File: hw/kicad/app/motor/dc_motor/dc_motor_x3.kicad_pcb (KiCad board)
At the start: 2 copper layers, 45 x 45 mm, 23 parts, among them J1 TOP, J3 Motor 2, J4 Motor 3, J6 BOTTUM, U1 DRV8870DDA, U2 DRV8870DDA, U3 DRV8870DDA

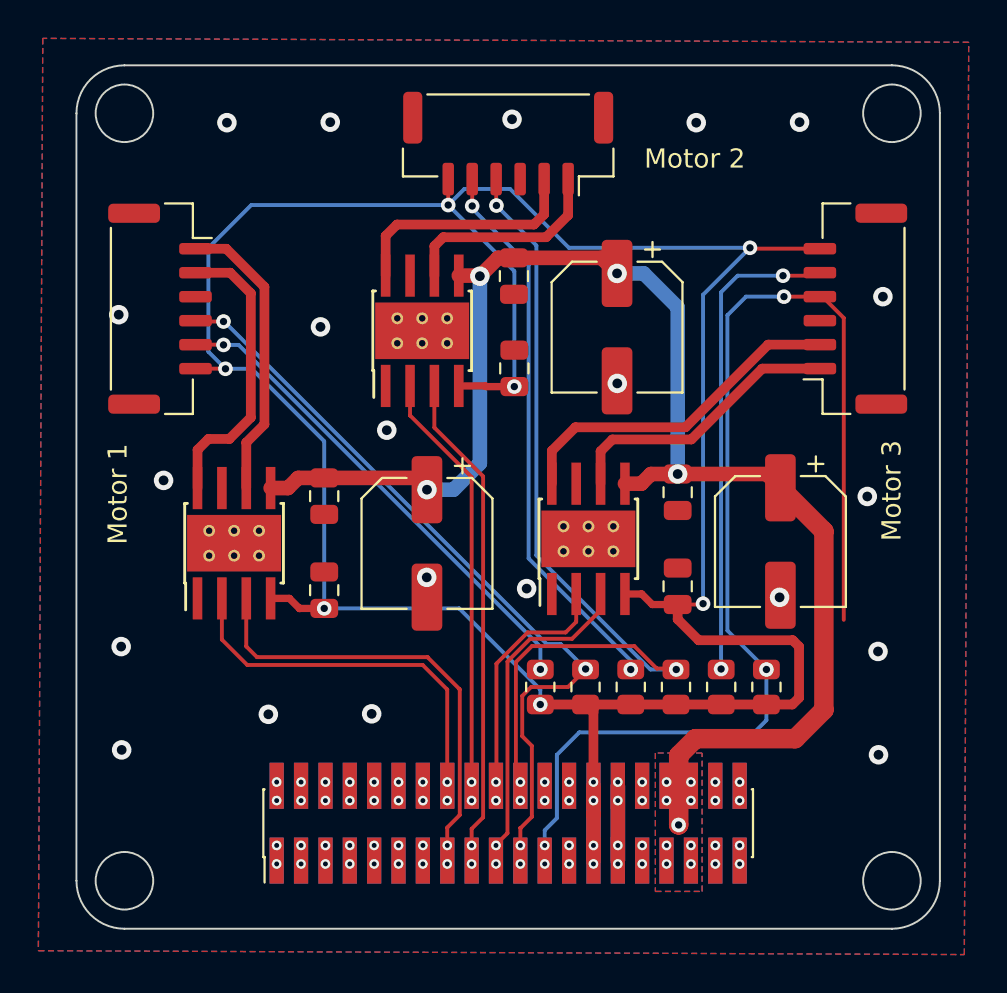
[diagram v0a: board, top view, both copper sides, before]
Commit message: 更换接口线序
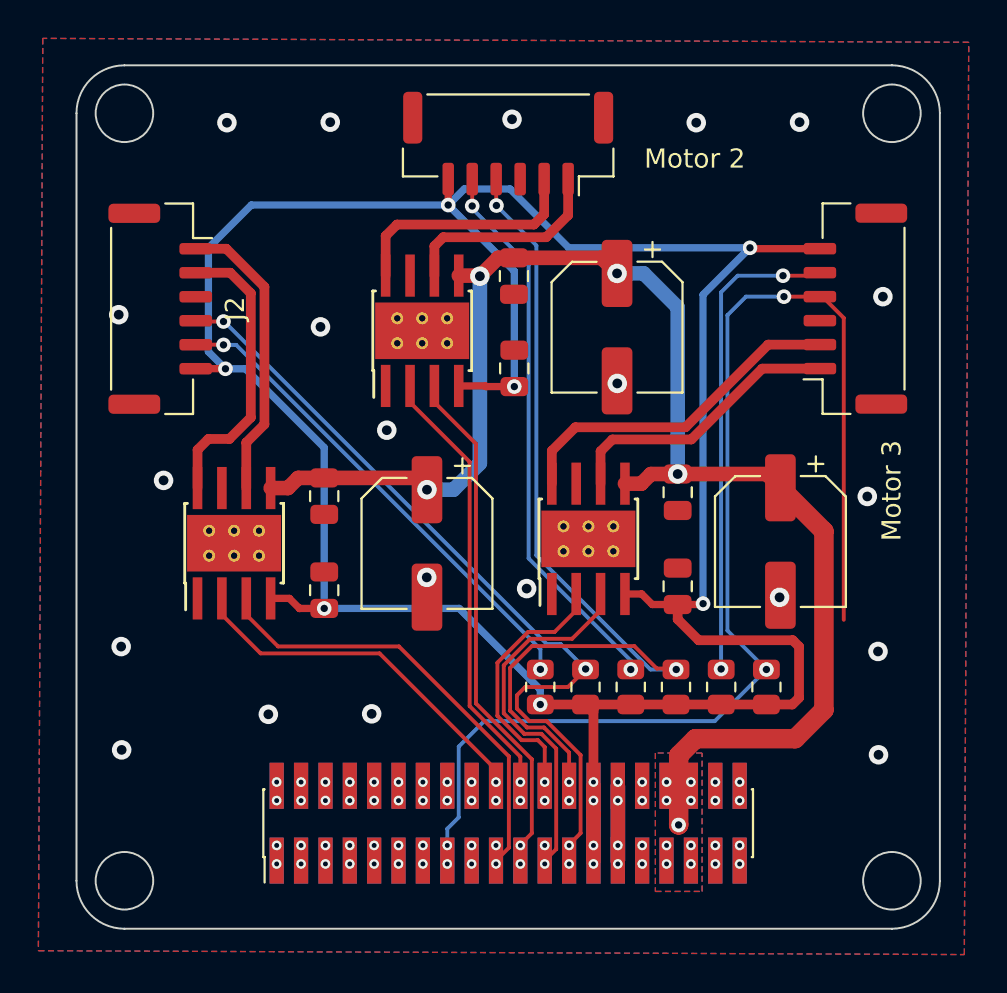
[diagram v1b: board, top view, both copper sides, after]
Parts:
- removed J: Motor 1, Connector_JST:JST_GH_SM06B-GHS-TB_1x06-1MP_P1.25mm_Horizontal
- added J2: Motor 1, Connector_JST:JST_GH_SM06B-GHS-TB_1x06-1MP_P1.25mm_Horizontal, F.Cu at (57.6, 48.4)
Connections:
- J1 pad 15: /GPIO_1 -> /CAN_H
- J1 pad 16: /GPIO_2 -> /CAN_L
- J1 pad 17: /GPIO_3 -> /USB+
- J1 pad 18: /GPIO_4 -> /USB-
- J1 pad 19: /GPIO_5 -> /GPIO_1
- J1 pad 20: /GPIO_6 -> /GPIO_2
- J1 pad 21: /ENC_1B -> /GPIO_3
- J1 pad 22: /ENC_2B -> /GPIO_4
- J1 pad 23: /CAN_H -> /GPIO_5
- J1 pad 24: /CAN_L -> /GPIO_6
- J1 pad 25: /USB+ -> /ENC_1B
- J1 pad 26: /USB- -> /ENC_2B
- J6 pad 15: /GPIO_2 -> /CAN_L
- J6 pad 16: /GPIO_1 -> /CAN_H
- J6 pad 17: /GPIO_4 -> /USB-
- J6 pad 18: /GPIO_3 -> /USB+
- J6 pad 19: /GPIO_6 -> /GPIO_2
- J6 pad 20: /GPIO_5 -> /GPIO_1
- J6 pad 21: /ENC_2B -> /GPIO_4
- J6 pad 22: /ENC_1B -> /GPIO_3
- J6 pad 23: /CAN_L -> /GPIO_6
- J6 pad 24: /CAN_H -> /GPIO_5
- J6 pad 25: /USB- -> /ENC_2B
- J6 pad 26: /USB+ -> /ENC_1B
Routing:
- net /CAN_H: track 62.1 -> 65.1 mm
- net /ENC_1B: track 40.8 -> 42.8 mm
- net /ENC_2B: track 46.0 -> 47.8 mm
- net /GPIO_5: track 17.4 -> 19.2 mm
- net /GPIO_4: track 22.2 -> 23.5 mm
- net /GPIO_6: track 12.9 -> 14.0 mm
- net /GPIO_3: track 26.0 -> 27.1 mm
- net /GPIO_2: track 20.0 -> 19.3 mm
